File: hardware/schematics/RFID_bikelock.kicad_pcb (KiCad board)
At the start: 2 copper layers, 35 parts, among them J1 BATT_IN, J2 USB_prog, J3 USB_battery, J4 BATT_CHRG, M1 Stepper_Motor_unipolar_5pin, SW1 SW_Push, SW2 SW_Push, U1 ULN2003, U2 ESP32-S3-WROOM-1, U3 ADPL40502AUJZ-3.3-R7, U4 MIC2288, U5 MCP73831-2-OT

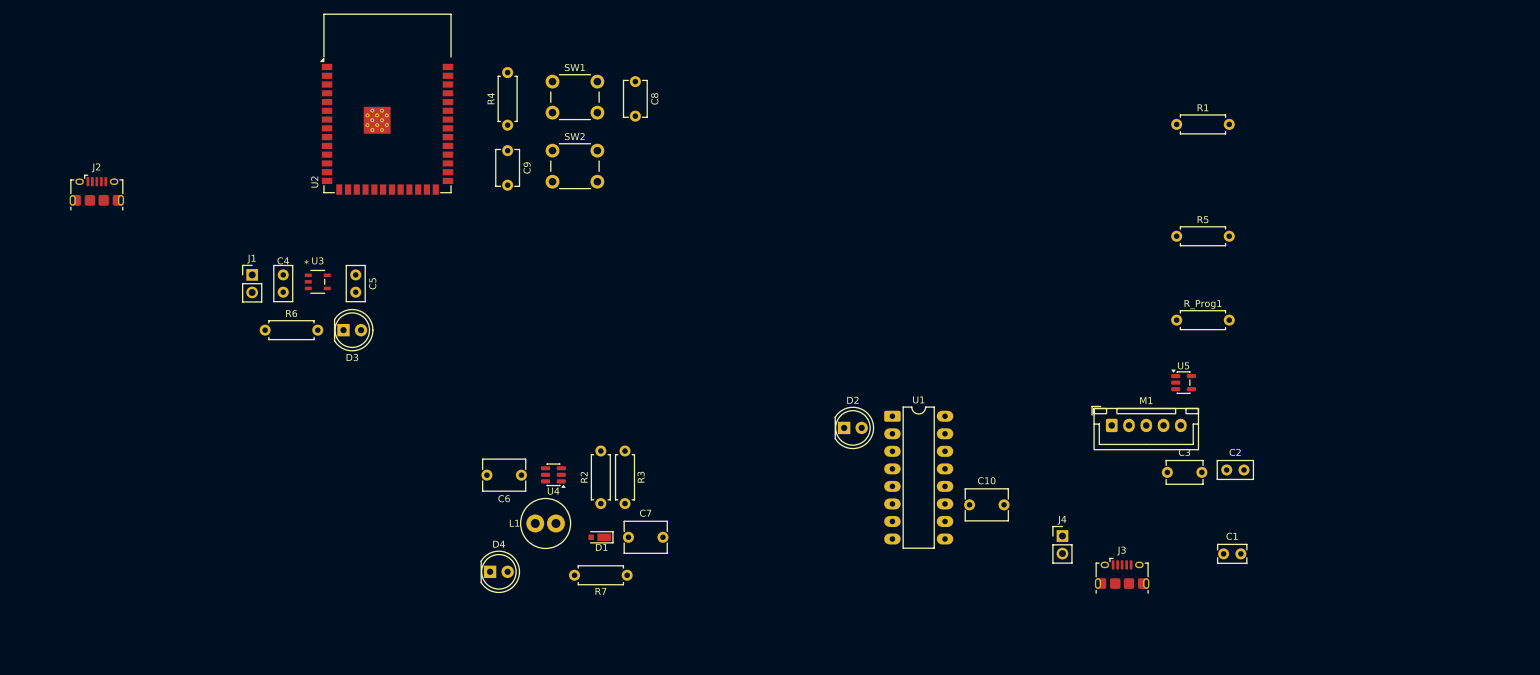
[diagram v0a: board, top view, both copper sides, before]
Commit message: Finished PCB placement. Need revision and edge cuts for break-off boards. Need to route tracks
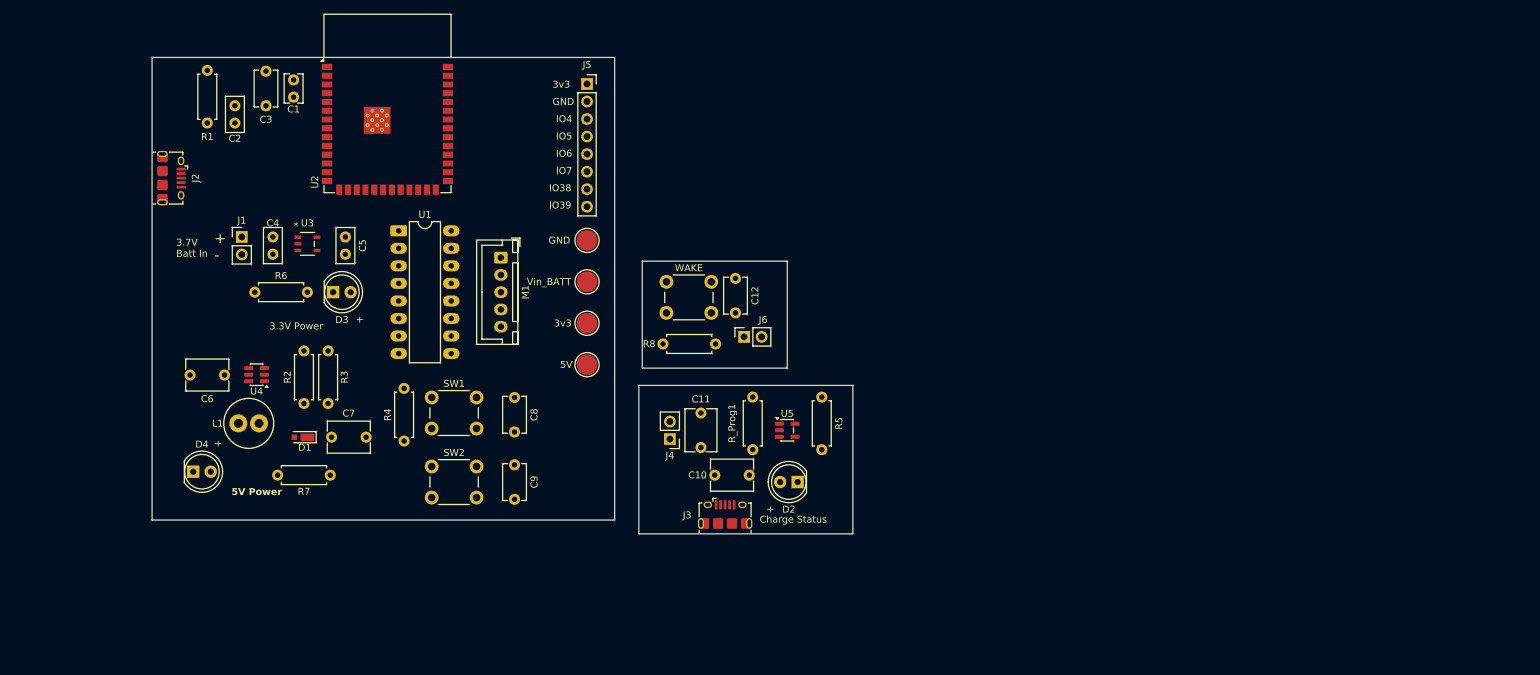
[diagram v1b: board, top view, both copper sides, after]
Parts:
- added 3v3: 3V3, TestPoint:TestPoint_Pad_D3.0mm, F.Cu at (134.0, 116.5)
- added 5V: 5V, TestPoint:TestPoint_Pad_D3.0mm, F.Cu at (134.0, 122.5)
- added C11: 4.7uF, Capacitor_THT:C_Disc_D6.0mm_W4.4mm_P5.00mm, F.Cu at (150.5, 134.5)
- added C12: 0.1uF, Capacitor_THT:C_Disc_D5.1mm_W3.2mm_P5.00mm, F.Cu at (155.5, 110.0)
- added GND: GND, TestPoint:TestPoint_Pad_D3.0mm, F.Cu at (134.0, 104.5)
- added J5: GPIO out, Connector_PinSocket_2.54mm:PinSocket_1x08_P2.54mm_Vertical, F.Cu at (134.0, 81.8)
- added J6: WAKE_IN_OUT, Connector_PinSocket_2.54mm:PinSocket_1x02_P2.54mm_Vertical, F.Cu at (156.8, 118.5)
- added R8: 1k, Resistor_THT:R_Axial_DIN0207_L6.3mm_D2.5mm_P7.62mm_Horizontal, F.Cu at (145.0, 119.5)
- added Vin_BATT: Batt In, TestPoint:TestPoint_Pad_D3.0mm, F.Cu at (134.0, 110.5)
- added WAKE: WAKE, Button_Switch_THT:SW_PUSH_6mm, F.Cu at (145.5, 110.5)
- SW1: value SW_Push -> EN
- SW2: value SW_Push -> BOOT
- moved C2 152.2 mm to (83.0, 87.5), turned to 90 degrees
- moved C1 151.2 mm to (91.5, 81.2), turned to -90 degrees
- moved C3 142.9 mm to (87.5, 80.0), turned to -90 degrees
- moved R1 140.6 mm to (79.0, 79.9), turned to -90 degrees
- moved M1 91.8 mm to (121.5, 107.0), turned to -90 degrees
- moved U1 76.4 mm to (106.7, 103.1)
- moved R_Prog1 62.4 mm to (158.0, 127.2), turned to -90 degrees
- moved R5 60.0 mm to (168.0, 134.8), turned to 90 degrees
- moved J4 58.6 mm to (146.0, 133.3), turned to 180 degrees
- moved J3 58.2 mm to (154.0, 144.2)
- moved U5 57.8 mm to (163.0, 132.0)
- moved C8 49.0 mm to (123.5, 127.2)
- moved SW1 49.0 mm to (111.5, 127.2)
- moved SW2 49.0 mm to (111.5, 137.2)
- moved R4 48.1 mm to (107.5, 133.6)
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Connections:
- M1 pad 2: Net-(U1-O2) -> Net-(U1-O1)
- U1 pad 15: Net-(U1-O2) -> Net-(M1--)
- U1 pad 16: Net-(M1--) -> Net-(U1-O1)
- U2 pad 10: unconnected-(U2-IO17-Pad10) -> /STEP2
- U2 pad 11: unconnected-(U2-IO18-Pad11) -> /STEP3
- U2 pad 18: /Boost_EN -> unconnected-(U2-IO10-Pad18)
- U2 pad 19: /STEP1 -> unconnected-(U2-IO11-Pad19)
- U2 pad 20: /STEP3 -> unconnected-(U2-IO12-Pad20)
- U2 pad 21: /STEP2 -> unconnected-(U2-IO13-Pad21)
- U2 pad 22: /STEP4 -> unconnected-(U2-IO14-Pad22)
- U2 pad 23: unconnected-(U2-IO21-Pad23) -> /STEP4
- U2 pad 31: unconnected-(U2-IO38-Pad31) -> /IO38
- U2 pad 32: unconnected-(U2-IO39-Pad32) -> /IO39
- U2 pad 4: unconnected-(U2-IO4-Pad4) -> /IO4
- U2 pad 5: unconnected-(U2-IO5-Pad5) -> /IO5
- U2 pad 6: unconnected-(U2-IO6-Pad6) -> /IO6
- U2 pad 7: unconnected-(U2-IO7-Pad7) -> /IO7
- U2 pad 8: unconnected-(U2-IO15-Pad8) -> /Boost_EN
- U2 pad 9: unconnected-(U2-IO16-Pad9) -> /STEP1
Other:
- board outline added: 101.5 x 69 mm
- board text added: "+"
- board text added: "+ -"
- board text added: "3.3V Power"
- board text added: "3.7V Batt In"
- board text added: "3v3"
- board text added: "5V Power"
- board text added: "Charge Status"
- board text added: "GND"
- board text added: "IO38"
- board text added: "IO39"
- board text added: "IO4"
- board text added: "IO5"
- board text added: "IO6"
- board text added: "IO7"

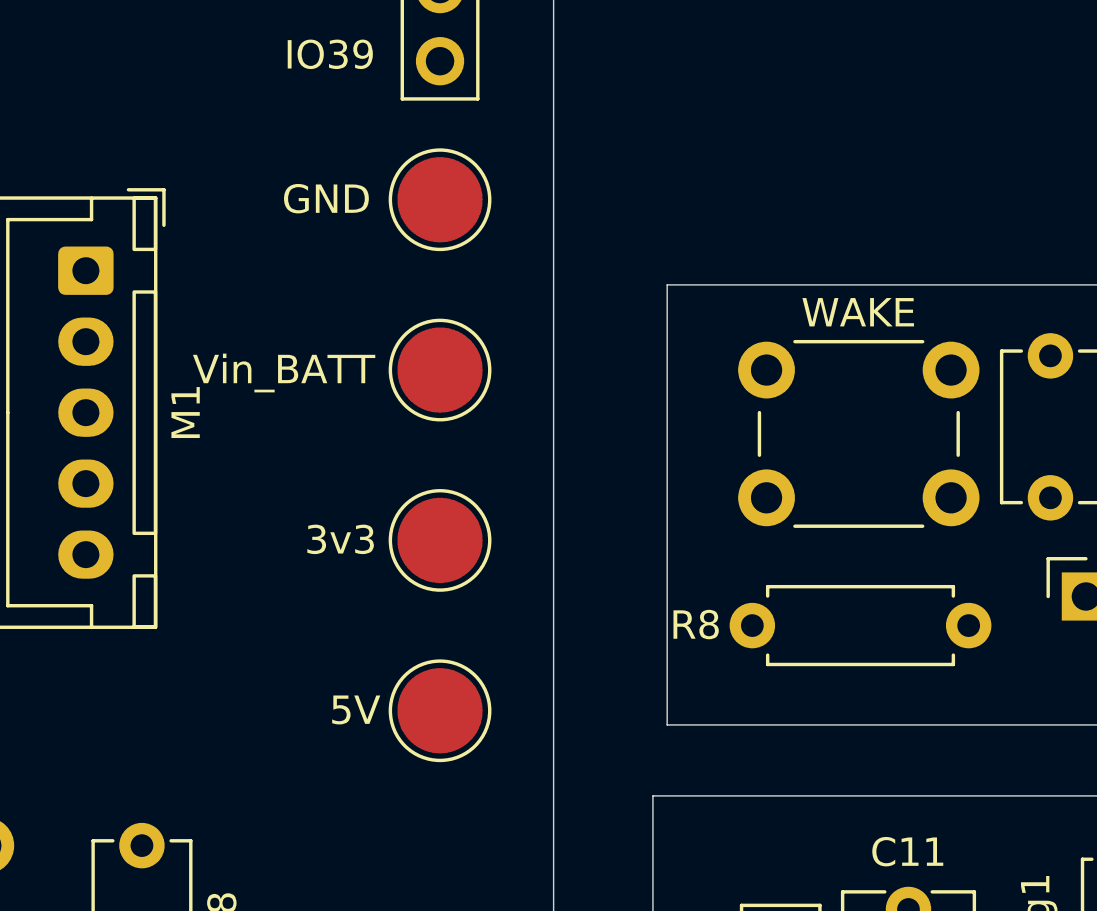
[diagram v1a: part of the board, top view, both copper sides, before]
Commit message: Made schematic cleaner - added sections and more description. Ran ERC check and dealt with most of the errors involving power pins.
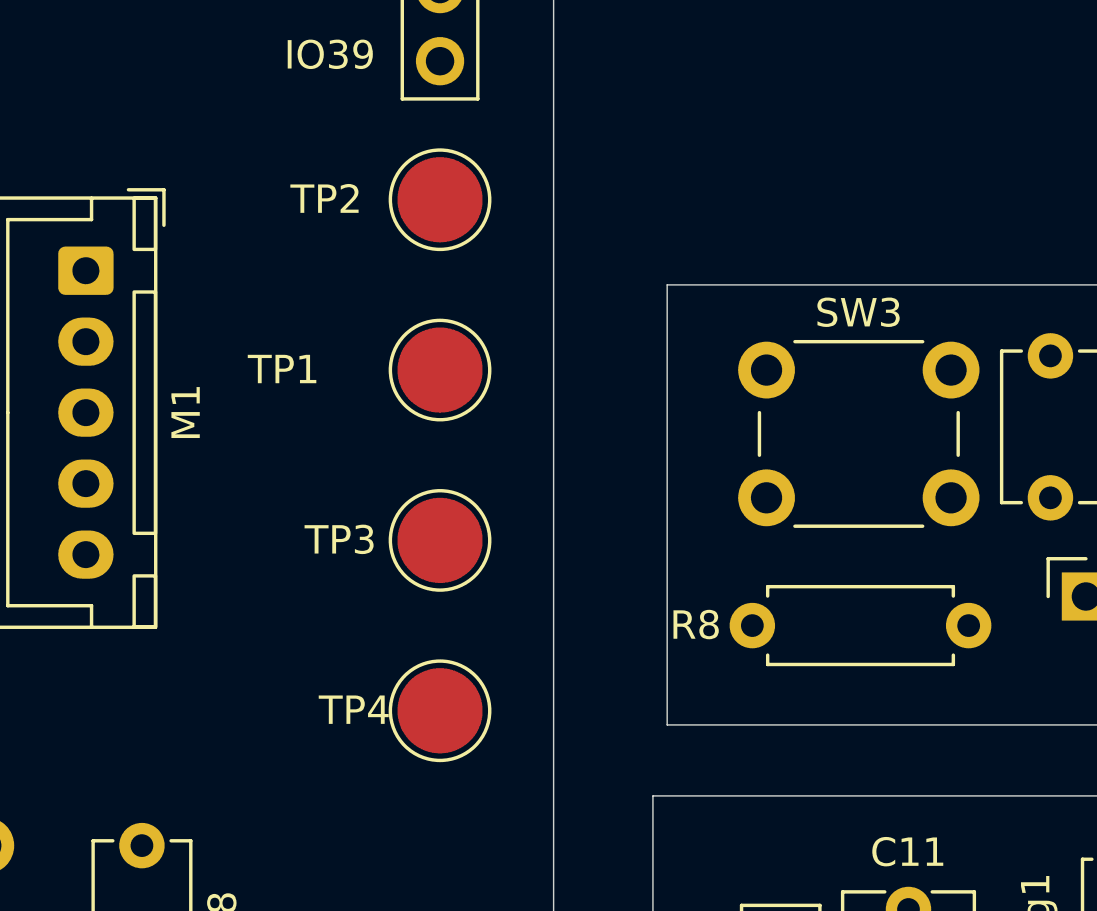
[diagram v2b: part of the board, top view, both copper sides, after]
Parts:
- renumbered WAKE to SW3, Vin_BATT to TP1, GND to TP2, 3v3 to TP3, 5V to TP4
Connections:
- net VBUS renamed /V_BATT
- M1 pad 2: Net-(U1-O1) -> +5V
- M1 pad 3: Net-(M1--) -> +5V
- M1 pad 4: Net-(U1-O3) -> +5V
- U1 pad 14: Net-(U1-O3) -> +5V
- U1 pad 15: Net-(M1--) -> +5V
- U1 pad 16: Net-(U1-O1) -> +5V

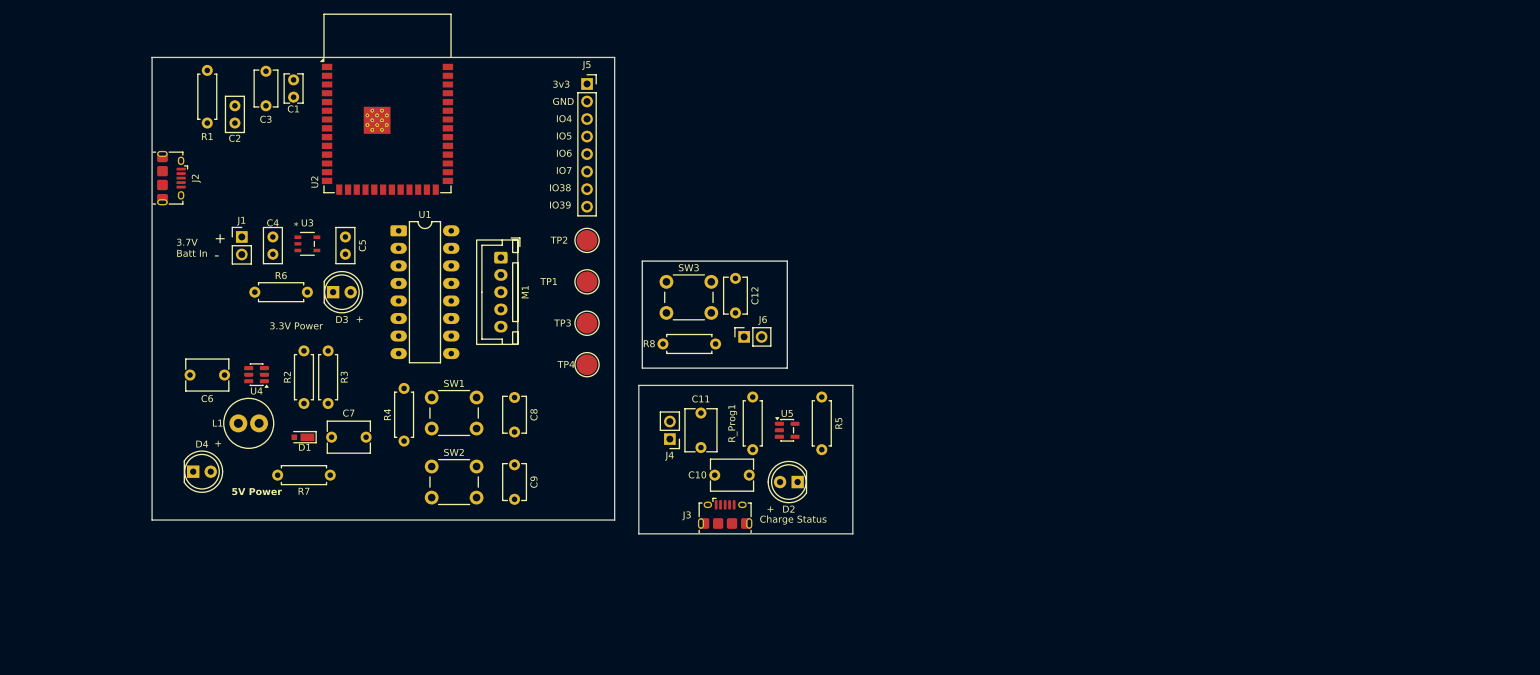
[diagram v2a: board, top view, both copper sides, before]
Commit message: Changes: change schematic to use power-path management battery charging, updated codebase to remove traces of old BLE involvement (moved to WIFI).     TODO: test deep sleep, fix power delivery in schematic (buck-boost for 5V power rail)
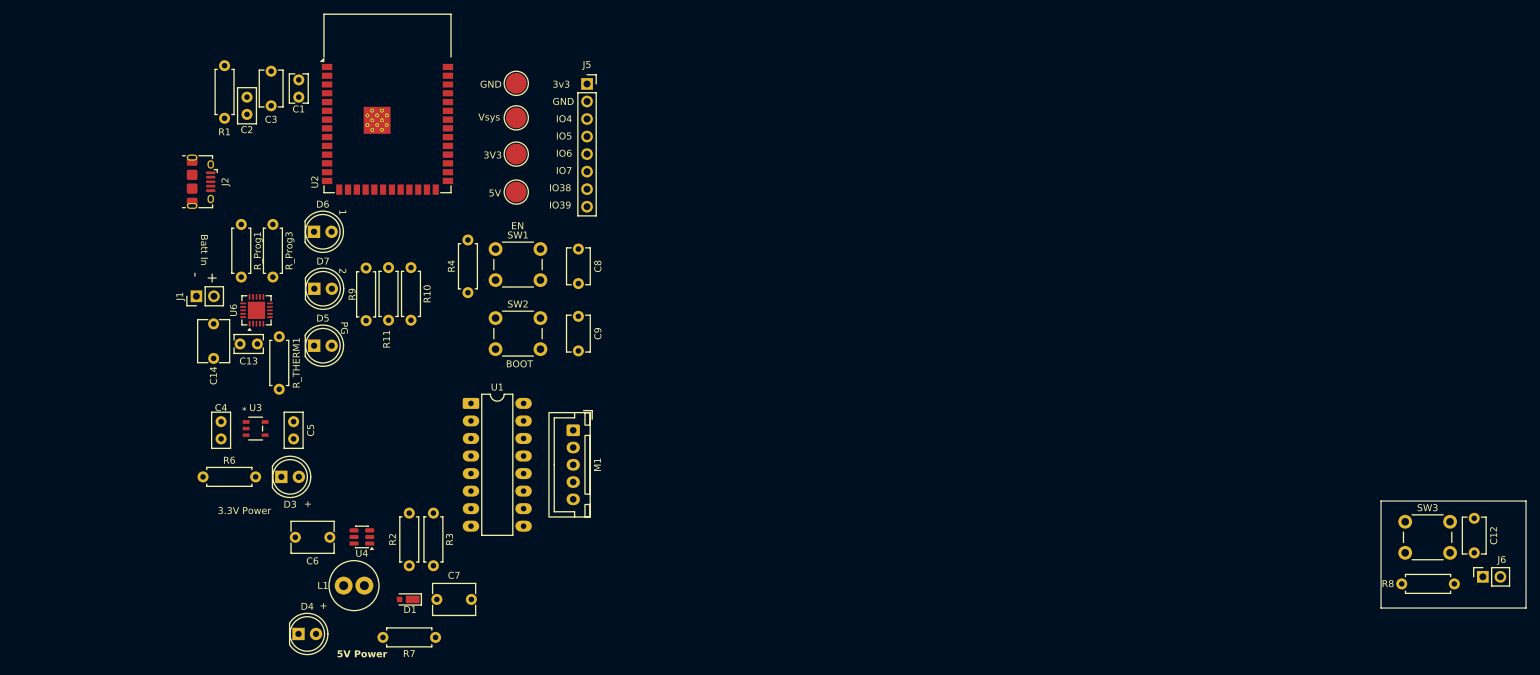
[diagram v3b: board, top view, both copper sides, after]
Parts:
- removed C10, C11: 4.7uF, Capacitor_THT:C_Disc_D6.0mm_W4.4mm_P5.00mm
- removed D2: CHRG-STAT, LED_THT:LED_D5.0mm
- removed J3: USB_battery, Connector_USB:USB_Micro-B_Amphenol_10118194_Horizontal
- removed J4: BATT_CHRG, Connector_PinHeader_2.54mm:PinHeader_1x02_P2.54mm_Vertical
- removed R5: 470, Resistor_THT:R_Axial_DIN0207_L6.3mm_D2.5mm_P7.62mm_Horizontal
- removed U5: MCP73831-2-OT, Package_TO_SOT_SMD:SOT-23-5
- added C13: 10 uF, Capacitor_THT:C_Rect_L4.0mm_W2.5mm_P2.50mm, F.Cu at (86.2, 119.5)
- added C14: 4.7uF, Capacitor_THT:C_Disc_D6.0mm_W4.4mm_P5.00mm, F.Cu at (79.9, 116.6)
- added D5: Pwr_Good, LED_THT:LED_D5.0mm, F.Cu at (94.5, 119.8)
- added D6: STAT1, LED_THT:LED_D5.0mm, F.Cu at (94.5, 103.2)
- added D7: STAT2, LED_THT:LED_D5.0mm, F.Cu at (94.5, 111.5)
- added R10: 470, Resistor_THT:R_Axial_DIN0207_L6.3mm_D2.5mm_P7.62mm_Horizontal, F.Cu at (108.5, 108.4)
- added R11: 470, Resistor_THT:R_Axial_DIN0207_L6.3mm_D2.5mm_P7.62mm_Horizontal, F.Cu at (105.2, 108.4)
- added R9: 470, Resistor_THT:R_Axial_DIN0207_L6.3mm_D2.5mm_P7.62mm_Horizontal, F.Cu at (102.0, 108.5)
- added R_Prog3: 20k, Resistor_THT:R_Axial_DIN0207_L6.3mm_D2.5mm_P7.62mm_Horizontal, F.Cu at (88.5, 102.2)
- added R_THERM1: 10k, Resistor_THT:R_Axial_DIN0207_L6.3mm_D2.5mm_P7.62mm_Horizontal, F.Cu at (89.4, 126.1)
- added U6: MCP73871-2CC, Package_DFN_QFN:QFN-20-1EP_4x4mm_P0.5mm_EP2.5x2.5mm, F.Cu at (86.1, 114.6)
- J1: value BATT_IN -> BATT_p2+
- R_Prog1: value 470 -> 2k
- moved C12 112.5 mm to (262.5, 144.8)
- moved J6 112.5 mm to (263.8, 153.2)
- moved R8 112.5 mm to (252.0, 154.2)
- moved SW3 112.5 mm to (252.5, 145.2)
- moved R_Prog1 78.2 mm to (83.9, 102.2)
- moved C6 28.0 mm to (96.8, 147.5)
- moved C7 28.0 mm to (112.2, 156.5)
- moved D1 28.0 mm to (107.9, 156.5)
- moved D4 28.0 mm to (92.2, 161.5)
- moved L1 28.0 mm to (98.8, 154.5)
- moved R2 28.0 mm to (108.2, 151.6)
- moved R3 28.0 mm to (111.8, 144.0)
- moved R7 28.0 mm to (112.1, 162.0)
- moved U4 28.0 mm to (101.4, 147.4)
- moved C4 27.8 mm to (81.0, 130.8)
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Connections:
- C4 pad 1: /V_BATT -> /Vsys
- C6 pad 1: /V_BATT -> /Vsys
- J1 pad 1: /V_BATT -> GND
- J1 pad 2: GND -> Net-(J1-Pin_2)
- J2 pad 1: /V_BATT -> /Vin
- L1 pad 1: /V_BATT -> /Vsys
- R_Prog1 pad 1: Net-(U5-PROG) -> GND
- R_Prog1 pad 2: GND2 -> Net-(U6-PROG1)
- TP1 pad 1: /V_BATT -> /Vsys
- U3 pad 1: /V_BATT -> /Vsys
- U3 pad 3: /V_BATT -> /Vsys
- U4 pad 5: /V_BATT -> /Vsys
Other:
- board size 101.5 x 69 mm -> 21 x 15.5 mm
- board text added: "1"
- board text added: "2"
- board text added: "3V3"
- board text added: "5V"
- board text added: "BOOT"
- board text added: "Batt In"
- board text added: "EN"
- board text added: "PG"
- board text added: "Vsys"
- board text removed: "3.7V Batt In"
- board text removed: "Charge Status"
